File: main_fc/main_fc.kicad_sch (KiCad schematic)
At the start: 0 parts

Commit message: updated TC routing
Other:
- sheet TC renamed TC0
- removed sheet ADC2
- added sheet ADC0 (adc.kicad_sch)
- sheet ADC1 ports: added AIN0, AIN1, AIN10, AIN11, AIN12, AIN13, AIN14, AIN15, AIN2, AIN3, AIN4, AIN5, AIN6, AIN7, AIN8, AIN9; removed none

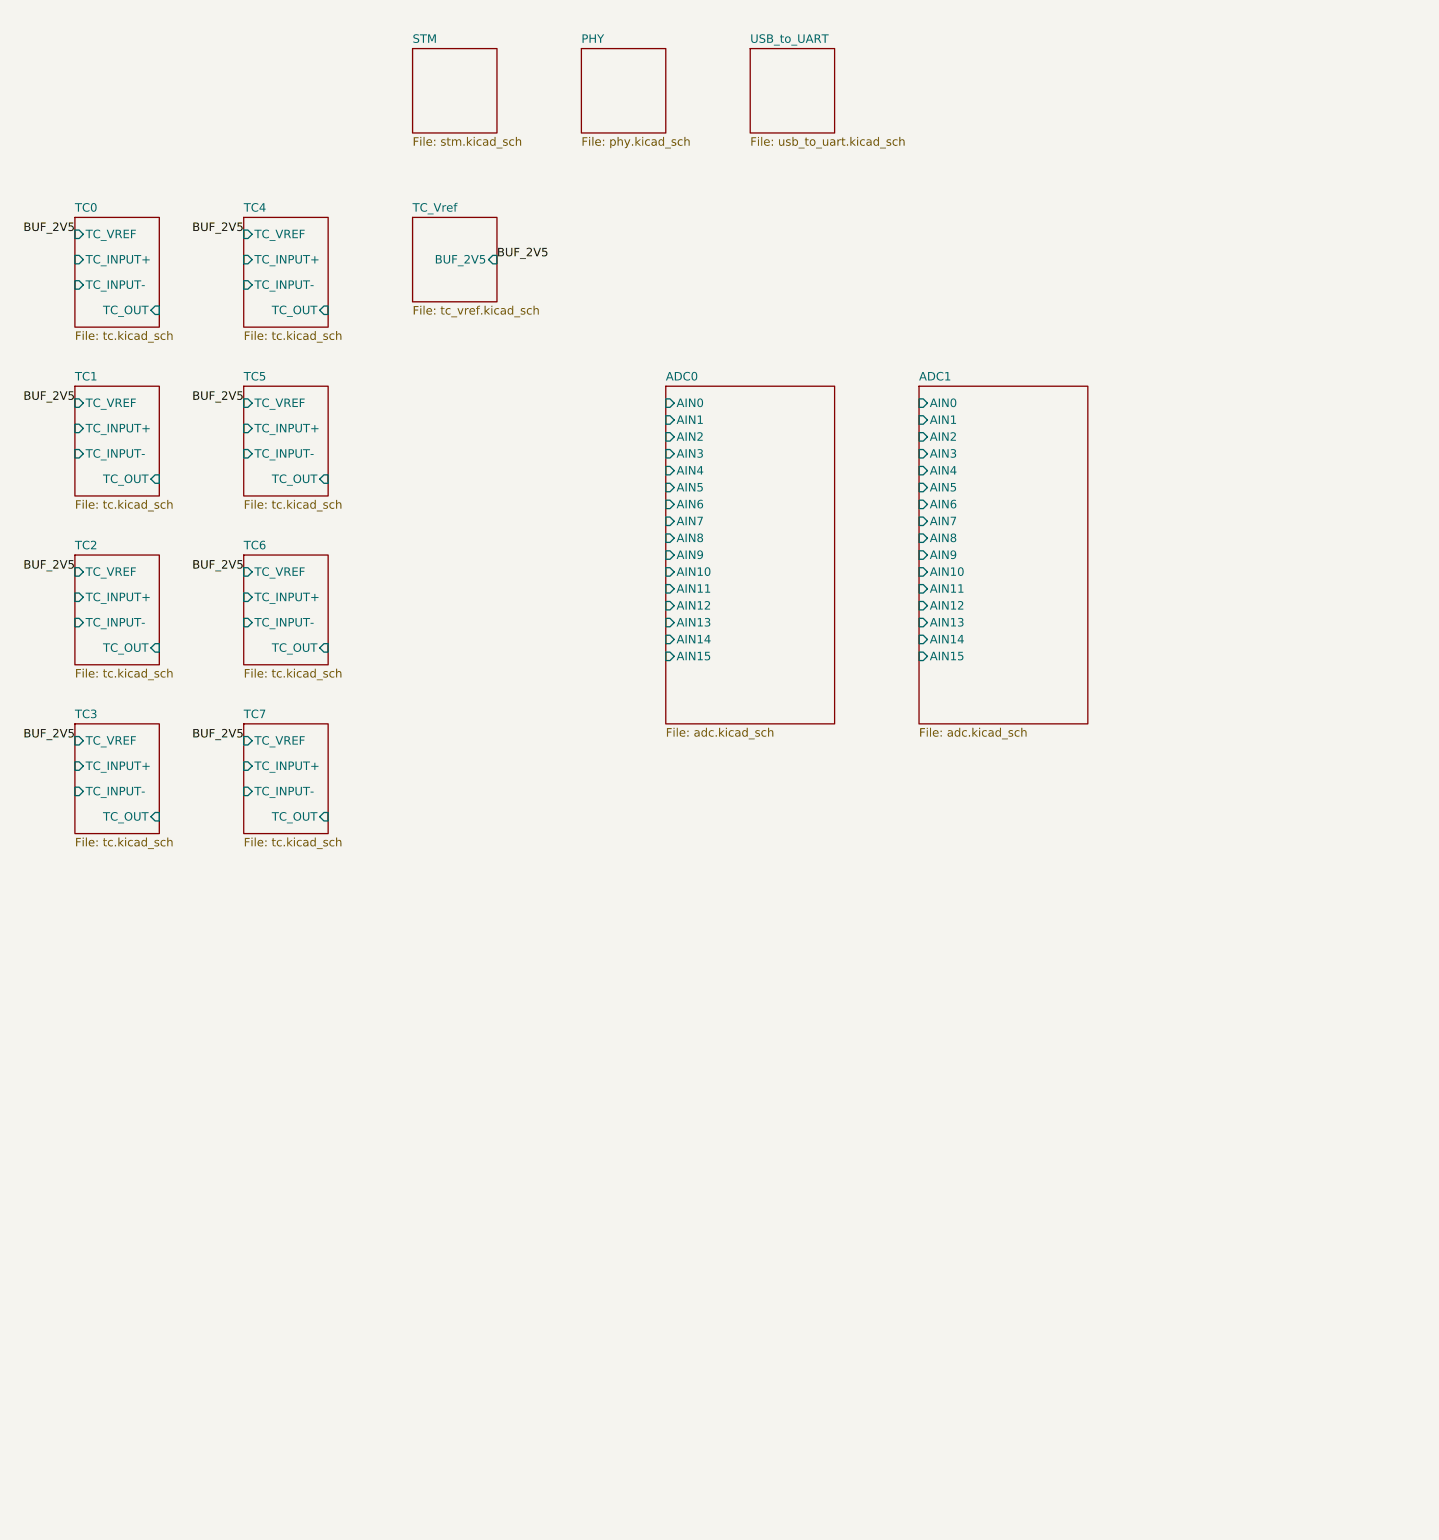
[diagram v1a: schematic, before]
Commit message: added pt dividers to schematic
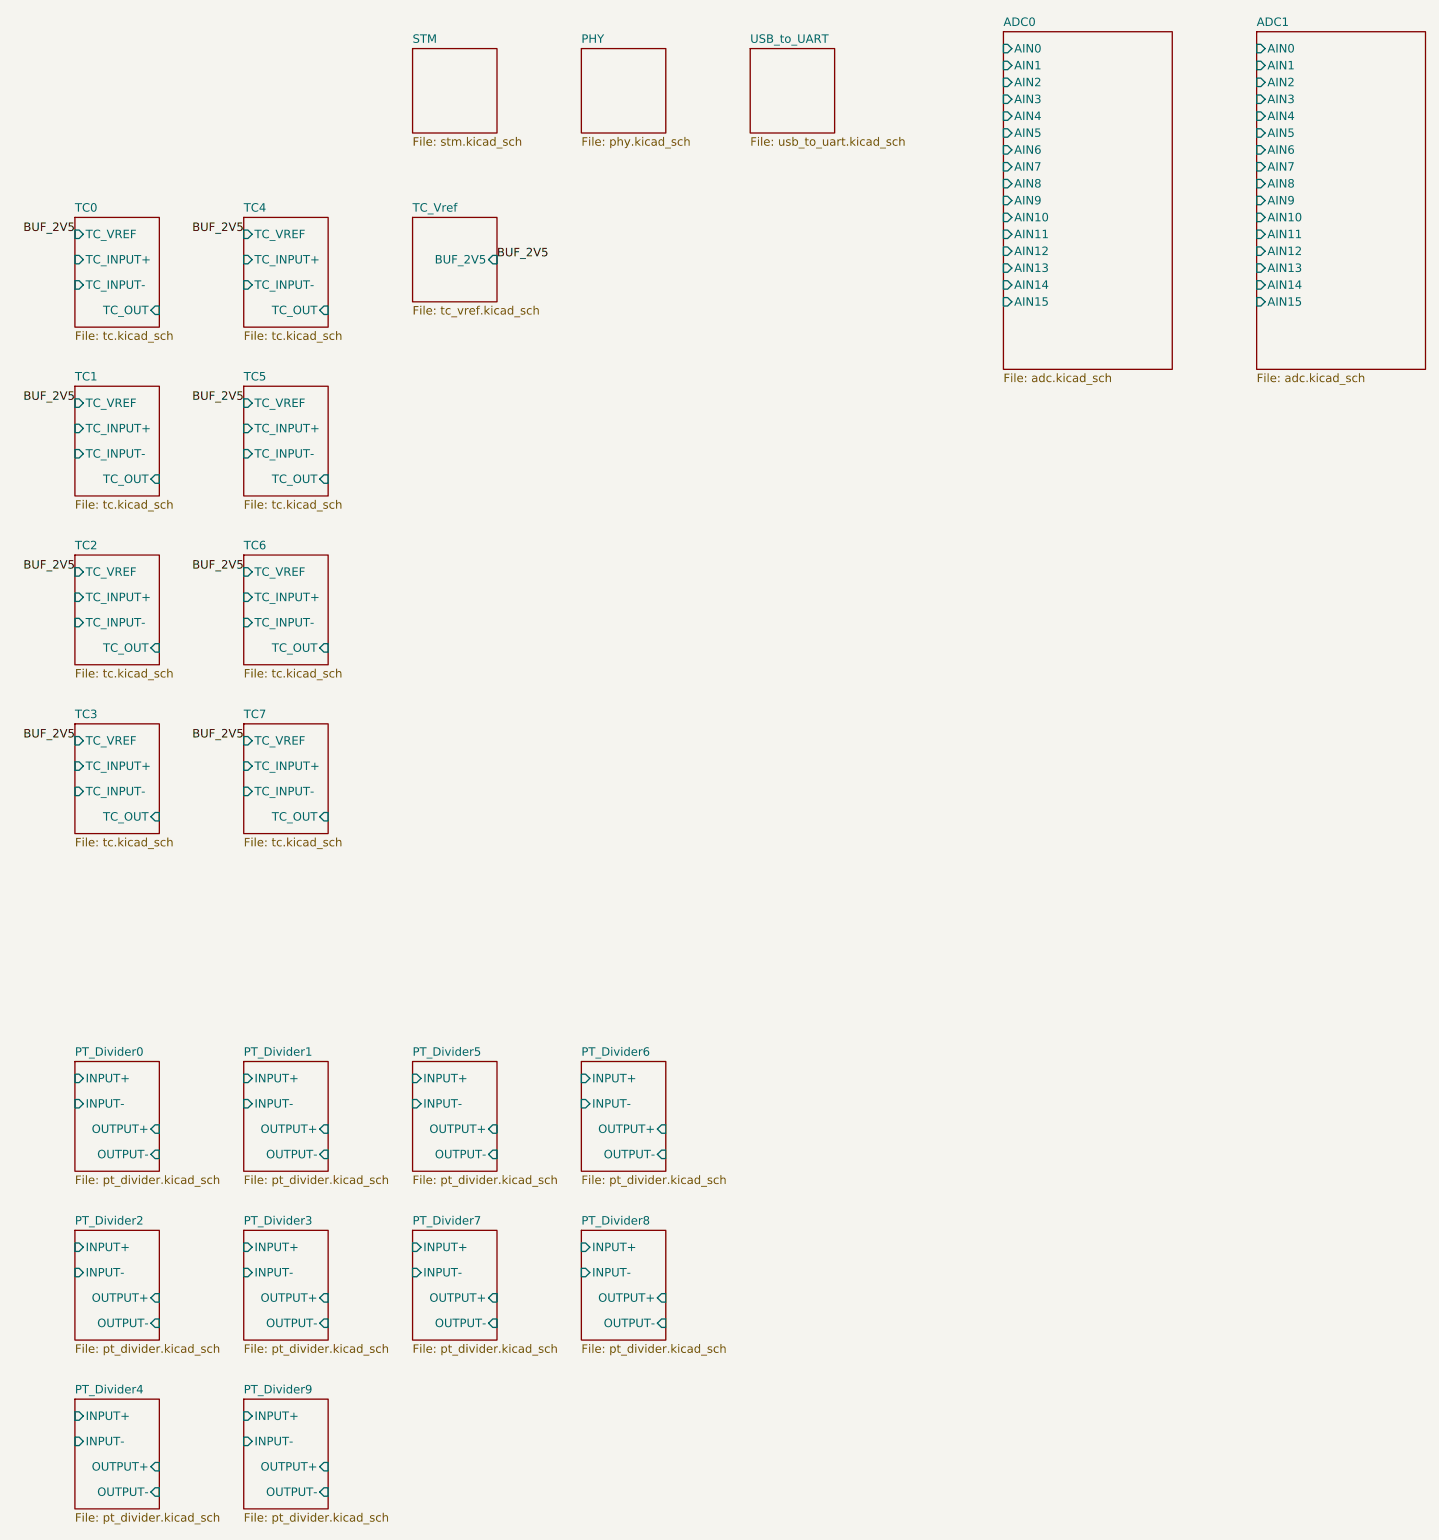
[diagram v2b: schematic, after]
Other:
- added sheet PT_Divider0 (pt_divider.kicad_sch)
- added sheet PT_Divider1 (pt_divider.kicad_sch)
- added sheet PT_Divider2 (pt_divider.kicad_sch)
- added sheet PT_Divider3 (pt_divider.kicad_sch)
- added sheet PT_Divider4 (pt_divider.kicad_sch)
- added sheet PT_Divider5 (pt_divider.kicad_sch)
- added sheet PT_Divider6 (pt_divider.kicad_sch)
- added sheet PT_Divider7 (pt_divider.kicad_sch)
- added sheet PT_Divider8 (pt_divider.kicad_sch)
- added sheet PT_Divider9 (pt_divider.kicad_sch)
